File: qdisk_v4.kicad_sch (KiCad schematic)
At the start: 31 parts, among them J1 QL_SLOT_DIN41612_CARD, J2 Conn_02x17_Odd_Even, Q1 PN2222A, U1 7805, U3 LS03, U4 LS11, U6 LS04, U7 LS00, U8 LS240, U9 27C128, Y1 8Mhz

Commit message: Add manual, 3d case and small corrections
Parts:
- C3: value 100n -> 330nf
- C9: value 27p -> 100n
- J1: footprint Connector_DIN:DIN41612_B_2x32_Male_Horizontal_THT -> 8bits:DIN41612_B_2x32_Female_Horizontal_THT
- RP1: value R_Network08 -> 4K7 (x4)
- RP2: value R_Network08 -> 2K2 (x6)
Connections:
- net FDC_IP renamed INDEX
- net FDC_T0 renamed TRACK_0
- net FDC_WRP renamed WRITE_PROT
- net NOSE_7 renamed A3N_PULLUP
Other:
- moved on the sheet: C1, C10, C11, C12, C13, C14, C2, C4, C5, C6, C7, U1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

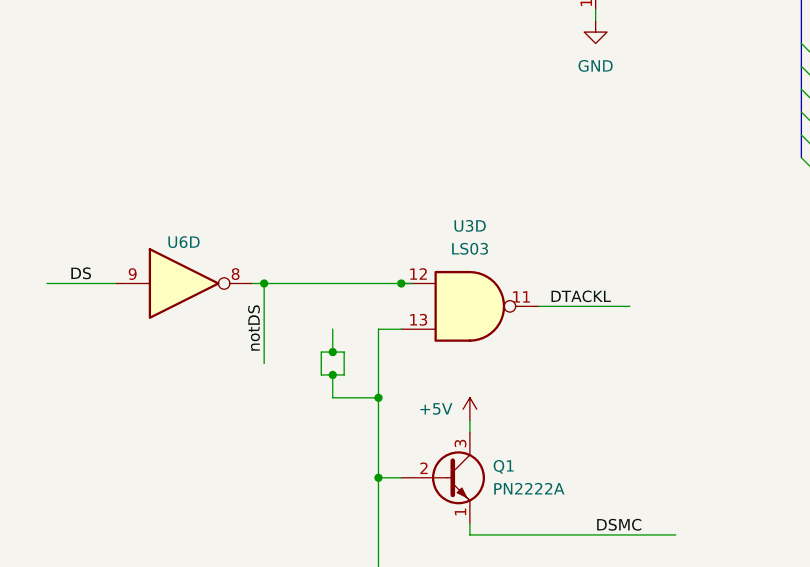
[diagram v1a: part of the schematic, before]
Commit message: Small corrections in the 3D model of the case
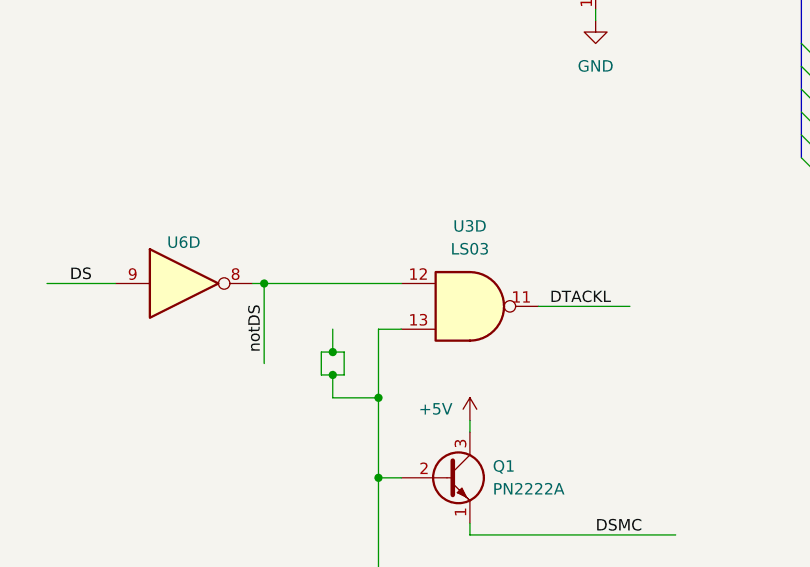
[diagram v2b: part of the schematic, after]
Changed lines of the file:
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@@
   (junction (at 22.86 256.54) (diameter 0) (color 0 0 0 0)
-  )
-  (junction (at 133.35 120.65) (diameter 0) (color 0 0 0 0)
   )
   (junction (at 77.47 266.7) (diameter 0) (color 0 0 0 0)
@@
     (stroke (width 0) (type default))
   )
-  (wire (pts (xy 133.35 120.65) (xy 134.62 120.65))
-    (stroke (width 0) (type default))
-  )
